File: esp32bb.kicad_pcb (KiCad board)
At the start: 2 copper layers, 43.2 x 61 mm, 33 parts, among them CON1 Micro_SD_Card, IC1 FT232RQ, P1 CONN_01X17, P2 CONN_01X17, P3 USB_OTG, Q1 MMBT3904, Q2 MMBT3904, SW1 SWITCH_SPST, SW2 SWITCH_SPST, U1 ESP32-WROOM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

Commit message: Add RX TX to headers
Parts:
- removed P2: CONN_01X17, common:Pin_Header_Straight_1x17_Pitch2.54mm
- added J1: CONN_01X18, common:Pin_Header_Straight_1x18_Pitch2.54mm, F.Cu at (190.5, 71.1)
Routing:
- net RXDtoTXD0: track 20.8 -> 39.3 mm
- net TXDtoRXD0: track 19.6 -> 36.0 mm
- net IO16: track 20.3 -> 24.4 mm
- net IO4: track 21.8 -> 25.8 mm
- net IO17: track 19.0 -> 22.8 mm
- net IO15: track 30.9 -> 34.5 mm, vias 0 -> 2
- net +3V3: track 135.5 -> 138.7 mm, vias 7 -> 6
- net IO5: track 18.5 -> 21.3 mm
- net IO19: track 17.4 -> 19.6 mm
- net IO21: track 17.4 -> 19.6 mm
- net IO18: track 18.0 -> 20.1 mm
- net IO2: track 64.4 -> 63.1 mm, vias 0 -> 4
- net VCC: track 23.8 -> 24.5 mm
- net GND: track 204.3 -> 204.6 mm, vias 9 -> 11
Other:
- board text added: "RX"
- board text added: "Rev 1.3"
- board text added: "TX"
- board text removed: "Rev 1.2"

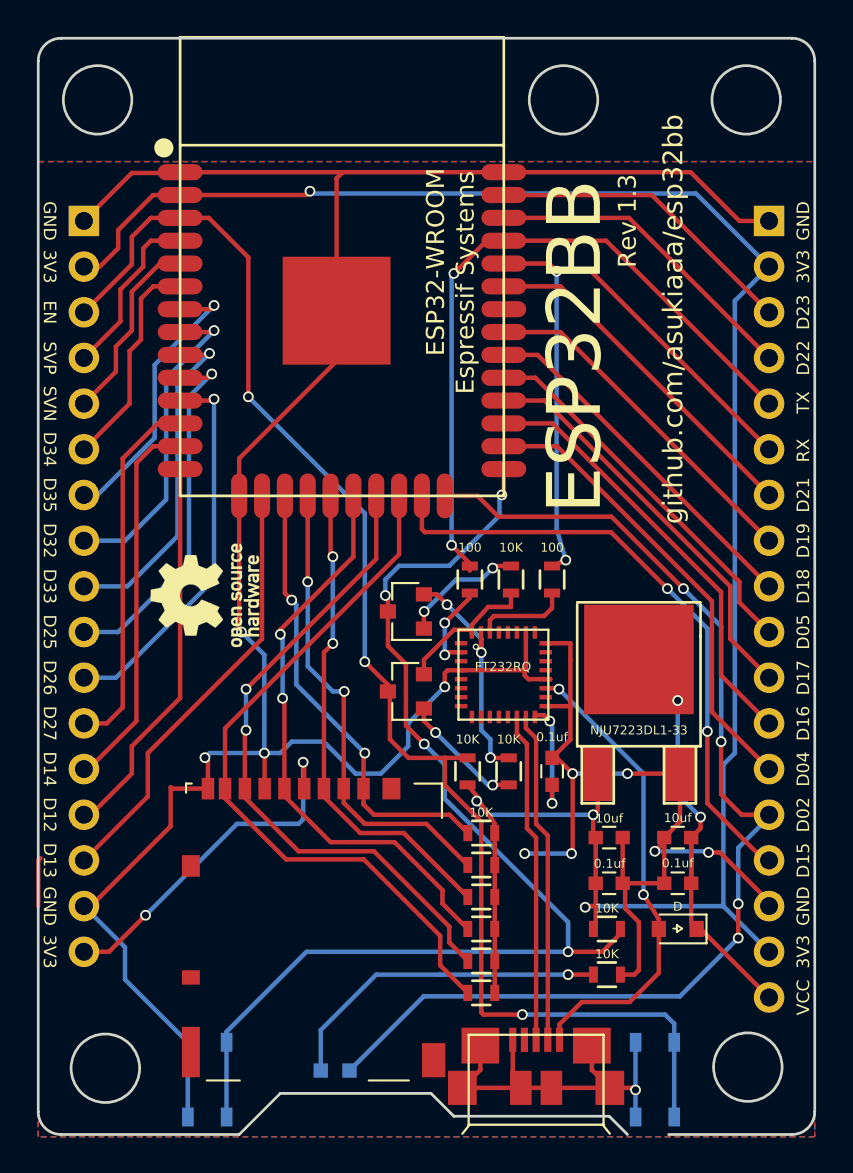
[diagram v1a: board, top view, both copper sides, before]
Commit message: Show component number on fab layer
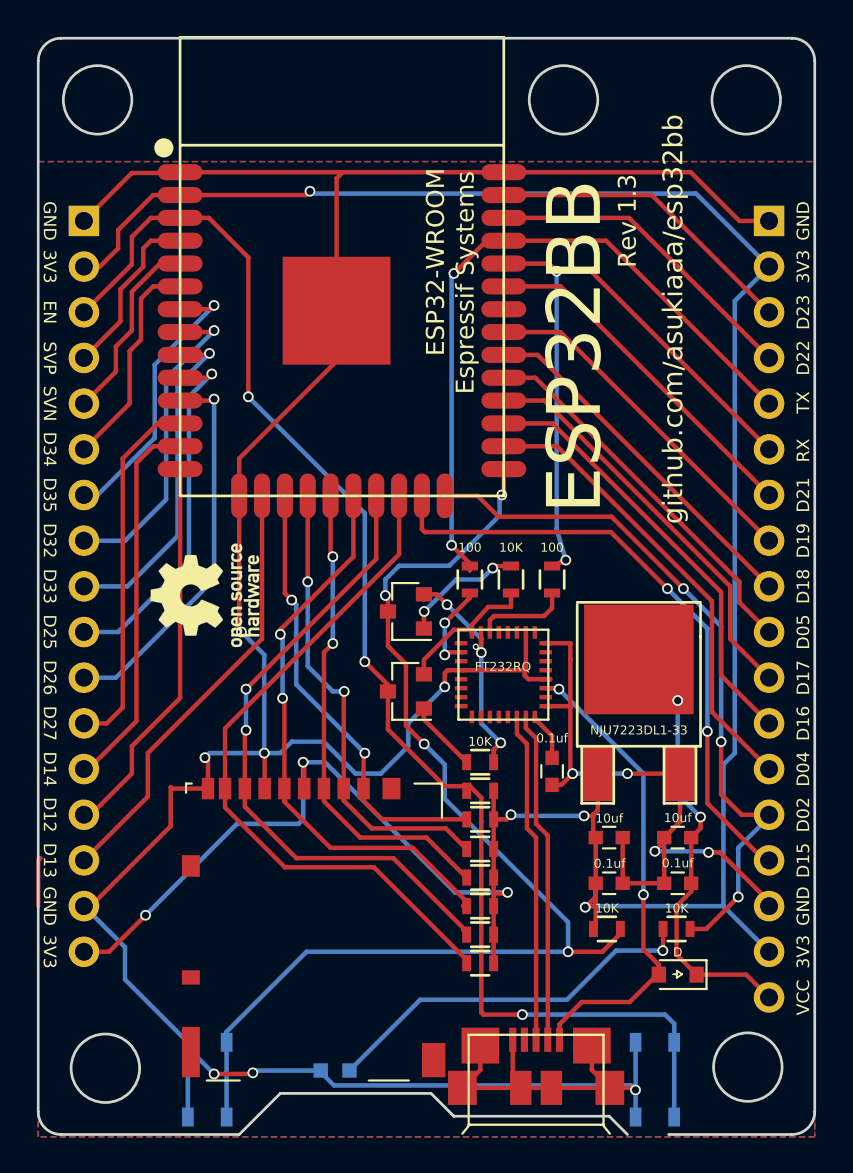
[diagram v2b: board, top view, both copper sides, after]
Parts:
- J1, P1: moved to B.Cu
- moved R7 4.63 mm to (185.4, 110.5), turned to 180 degrees
- moved D1 2.54 mm to (185.4, 113.0)
- moved R1 1.67 mm to (174.4, 101.2), turned to 180 degrees
- moved R8 1.65 mm to (174.4, 112.4)
- moved R9 1.46 mm to (174.4, 110.8)
- moved R3 1.29 mm to (174.4, 102.8), turned to 0 degrees
- moved R10 1.27 mm to (174.4, 109.2)
- moved R11 1.08 mm to (174.4, 107.6)
- moved R12 0.89 mm to (174.4, 106.0)
- moved R13 0.76 mm to (174.4, 104.4)
- turned C6 to 270 degrees
- turned J1 to 180 degrees
- turned P1 to 180 degrees
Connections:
- D2 pad 1: Net-(D2-Pad1) -> GND
- D2 pad 2: IO2 -> Net-(D2-Pad2)
- R7 pad 1: Net-(D2-Pad1) -> IO2
- R7 pad 2: GND -> Net-(D2-Pad2)
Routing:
- net IO2: track 63.1 -> 39.5 mm, vias 4 -> 3
- net Net-(D2-Pad2): track 0.00 -> 21.4 mm, vias 0 -> 1
- net Net-(D2-Pad1): track 18.7 -> 0.00 mm, vias 1 -> 0
- net GND: track 204.6 -> 218.3 mm
- net +3V3: track 138.7 -> 151.9 mm, vias 6 -> 7
- net Net-(C6-Pad1): track 6.75 -> 2.81 mm, vias 2 -> 0
- net Net-(Q1-Pad1): track 6.88 -> 3.97 mm, vias 2 -> 0
- net EN: track 79.1 -> 77.6 mm
- net SD1: track 39.8 -> 39.0 mm
- net SD_CMD: track 27.3 -> 28.0 mm
